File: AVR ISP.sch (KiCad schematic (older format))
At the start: 12 parts, among them CON1 AVR-ISP-6, IC1 ATMEGA328-P, IC2 ATTINY2313-P, IC3 ATTINY85-M, IC4 ATTINY2313-S

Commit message: Modified Schematic
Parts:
- removed IC3: ATTINY85-M, QFN/MLF20, symbol ATTINY85-M
- added IC3: ATTINY85-S, SO8-200, symbol ATTINY85-S
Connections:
- net +5V: now also IC3.8 (VCC)
- net GND: now also SHIELD1.GND3, IC3.4 (GND)
- net at CON1.5, IC1.1 ((PCINT14/~RESET~)PC6), IC2.1 (PA2(~RESET~/dW))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: now also IC3.1 (PB5(~RESET~/dW/ADC0/PCINT5))
- net at CON1.4, IC1.17 ((PCINT3/OC2A/MOSI)PB3), IC2.17 ((PCINT5/MOSI/DI/SDA)PB5)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: now also IC3.5 (PB0(MOSI/DI/SDA/AIN0/OC0A/OC1A/AREF/PCINT0))
- net at CON1.1, IC1.18 ((PCINT4/MISO)PB4), IC2.18 ((PCINT6/MISO/DO)PB6)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: now also IC3.6 (PB1(MISO/DO/AIN1/OC0B/OC1A/PCINT1))
- net at CON1.3, IC1.19 ((PCINT5/SCK)PB5), IC2.19 ((PCINT7/USCK/SCK/SCL)PB7)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: now also IC3.7 (PB2(SCK/USCK/SCL/T0/INT0/ADC1/PCINT2))
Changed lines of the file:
@@
-EESchema Schematic File Version 2  date 25/08/2013 21:04:07
+EESchema Schematic File Version 2  date 25/08/2013 22:06:19
 LIBS:power
 LIBS:device
@@
 Comment4 ""
 $EndDescr
+$Comp
+L GND #PWR01
+U 1 1 521A6D91
+P 6500 3800
+F 0 "#PWR01" H 6500 3800 30  0001 C CNN
+F 1 "GND" H 6500 3730 30  0001 C CNN
+	1    6500 3800
+	1    0    0    -1
+$EndComp
+$Comp
+L ATTINY85-S IC3
+U 1 1 521A67A5
+P 7800 2050
+F 0 "IC3" H 7900 2100 60  0000 C CNN
+F 1 "ATTINY85-S" H 9800 1300 60  0000 C CNN
+F 2 "SO8-200" H 8050 1300 60  0001 C CNN
+	1    7800 2050
+	1    0    0    -1
+$EndComp
 Wire Wire Line
 	4975 5950 4675 5950
@@
 	4775 5850 4975 5850
 $Comp
-L GND #PWR01
+L GND #PWR02
 U 1 1 521A5EF9
 P 5550 6100
-F 0 "#PWR01" H 5550 6100 30  0001 C CNN
+F 0 "#PWR02" H 5550 6100 30  0001 C CNN
 F 1 "GND" H 5550 6030 30  0001 C CNN
 	1    5550 6100
@@
 $EndComp
 $Comp
-L GND #PWR02
+L GND #PWR03
 U 1 1 521A5EEF
 P 4050 4500
-F 0 "#PWR02" H 4050 4500 30  0001 C CNN
+F 0 "#PWR03" H 4050 4500 30  0001 C CNN
 F 1 "GND" H 4050 4430 30  0001 C CNN
 	1    4050 4500
@@
 $EndComp
 $Comp
-L +5V #PWR03
+L +5V #PWR04
 U 1 1 521A5E82
 P 4450 3500
-F 0 "#PWR03" H 4450 3590 20  0001 C CNN
+F 0 "#PWR04" H 4450 3590 20  0001 C CNN
 F 1 "+5V" H 4450 3590 30  0000 C CNN
 	1    4450 3500
@@
 $EndComp
 $Comp
-L GND #PWR04
+L GND #PWR05
 U 1 1 521A5CF9
 P 3100 3100
-F 0 "#PWR04" H 3100 3100 30  0001 C CNN
+F 0 "#PWR05" H 3100 3100 30  0001 C CNN
 F 1 "GND" H 3100 3030 30  0001 C CNN
 	1    3100 3100
@@
 $EndComp
 $Comp
-L GND #PWR05
+L GND #PWR06
 U 1 1 521A5CF4
 P 6050 3100
-F 0 "#PWR05" H 6050 3100 30  0001 C CNN
+F 0 "#PWR06" H 6050 3100 30  0001 C CNN
 F 1 "GND" H 6050 3030 30  0001 C CNN
 	1    6050 3100
@@
 $EndComp
 $Comp
-L GND #PWR06
+L GND #PWR07
 U 1 1 521A5CED
 P 10300 2650
-F 0 "#PWR06" H 10300 2650 30  0001 C CNN
+F 0 "#PWR07" H 10300 2650 30  0001 C CNN
 F 1 "GND" H 10300 2580 30  0001 C CNN
 	1    10300 2650
@@
 $EndComp
 $Comp
-L GND #PWR07
+L GND #PWR08
 U 1 1 521A5B0E
 P 8550 5800
-F 0 "#PWR07" H 8550 5800 30  0001 C CNN
+F 0 "#PWR08" H 8550 5800 30  0001 C CNN
 F 1 "GND" H 8550 5730 30  0001 C CNN
 	1    8550 5800
@@
 $EndComp
 $Comp
-L GND #PWR08
+L GND #PWR09
 U 1 1 521A5B08
 P 8550 5700
-F 0 "#PWR08" H 8550 5700 30  0001 C CNN
+F 0 "#PWR09" H 8550 5700 30  0001 C CNN
 F 1 "GND" H 8550 5630 30  0001 C CNN
 	1    8550 5700
@@
 $EndComp
 $Comp
-L GND #PWR09
+L GND #PWR010
 U 1 1 521A5B03
 P 8000 5000
-F 0 "#PWR09" H 8000 5000 30  0001 C CNN
+F 0 "#PWR010" H 8000 5000 30  0001 C CNN
 F 1 "GND" H 8000 4930 30  0001 C CNN
 	1    8000 5000
@@
 $EndComp
 $Comp
-L GND #PWR010
+L GND #PWR011
 U 1 1 521A5AFA
 P 8000 4700
-F 0 "#PWR010" H 8000 4700 30  0001 C CNN
+F 0 "#PWR011" H 8000 4700 30  0001 C CNN
 F 1 "GND" H 8000 4630 30  0001 C CNN
 	1    8000 4700
@@
 $EndComp
 $Comp
-L GND #PWR011
+L GND #PWR012
 U 1 1 521A5AF3
 P 8000 4400
-F 0 "#PWR011" H 8000 4400 30  0001 C CNN
+F 0 "#PWR012" H 8000 4400 30  0001 C CNN
 F 1 "GND" H 8000 4330 30  0001 C CNN
 	1    8000 4400
@@
 	1    0    0    -1
 $EndComp
-$Comp
-L ATTINY85-M IC3
-U 1 1 520B9E29
-P 7800 2050
-F 0 "IC3" H 7900 2100 60  0000 C CNN
-F 1 "ATTINY85-M" H 9800 1300 60  0000 C CNN
-F 2 "QFN/MLF20" H 8100 1300 60  0001 C CNN
-	1    7800 2050
-	1    0    0    -1
-$EndComp

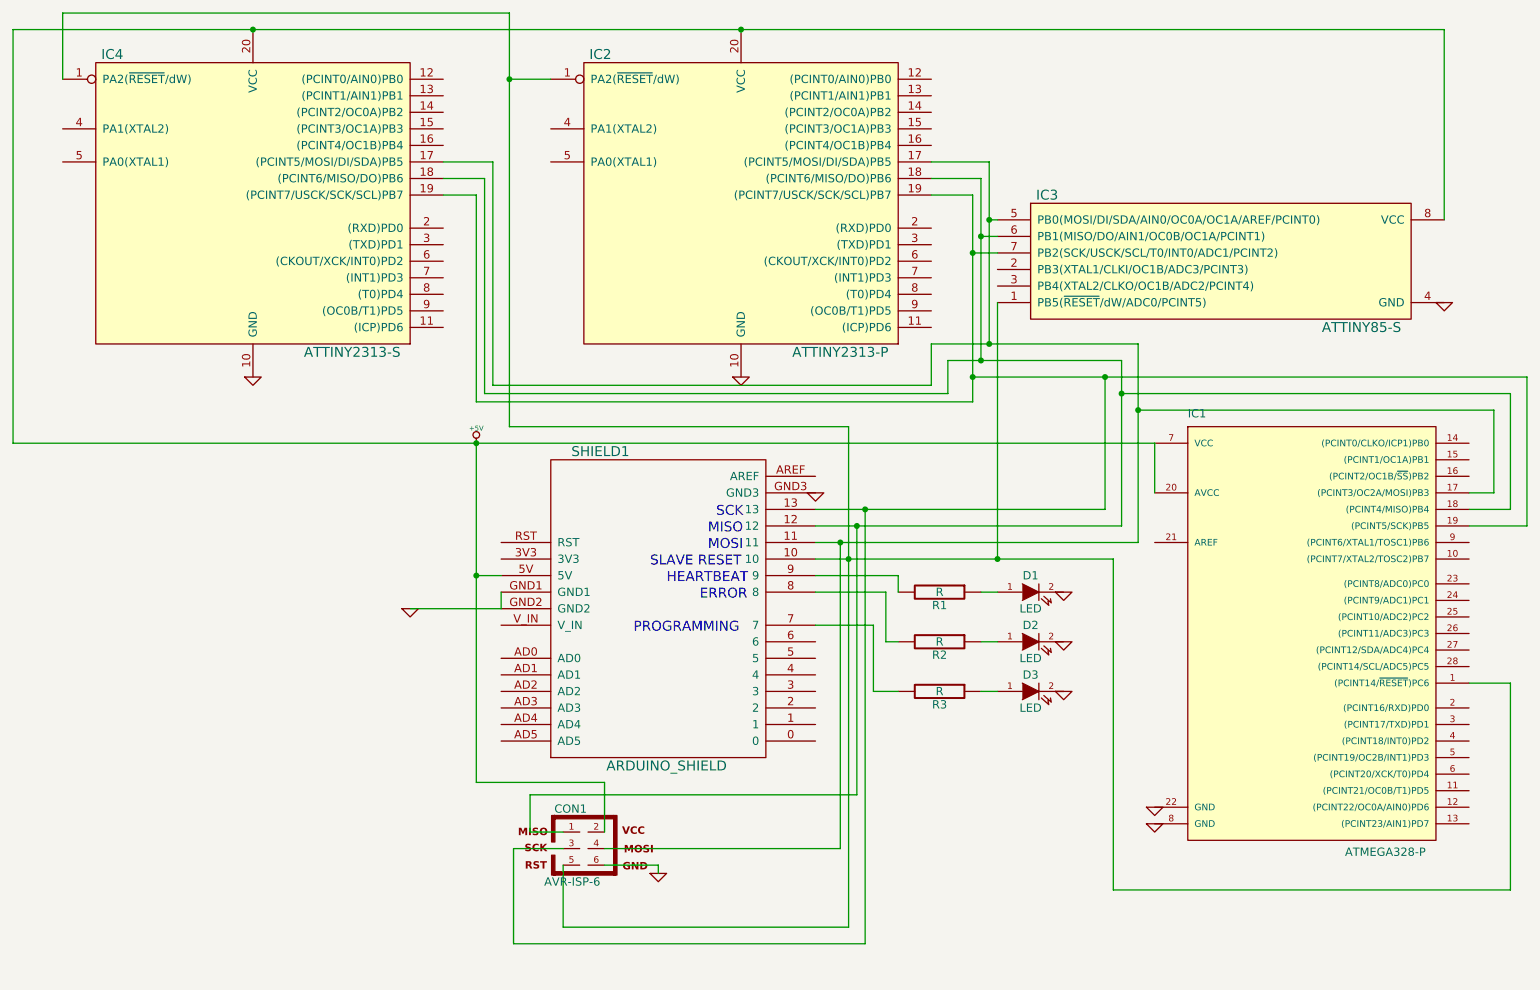
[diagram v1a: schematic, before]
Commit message: Logos added and ATTiny85 Moved.
Also added ground to the soic at pin 4 for ATTiny85 programming and
moved the ISP Headers to allow me to put a massive logo on the back.
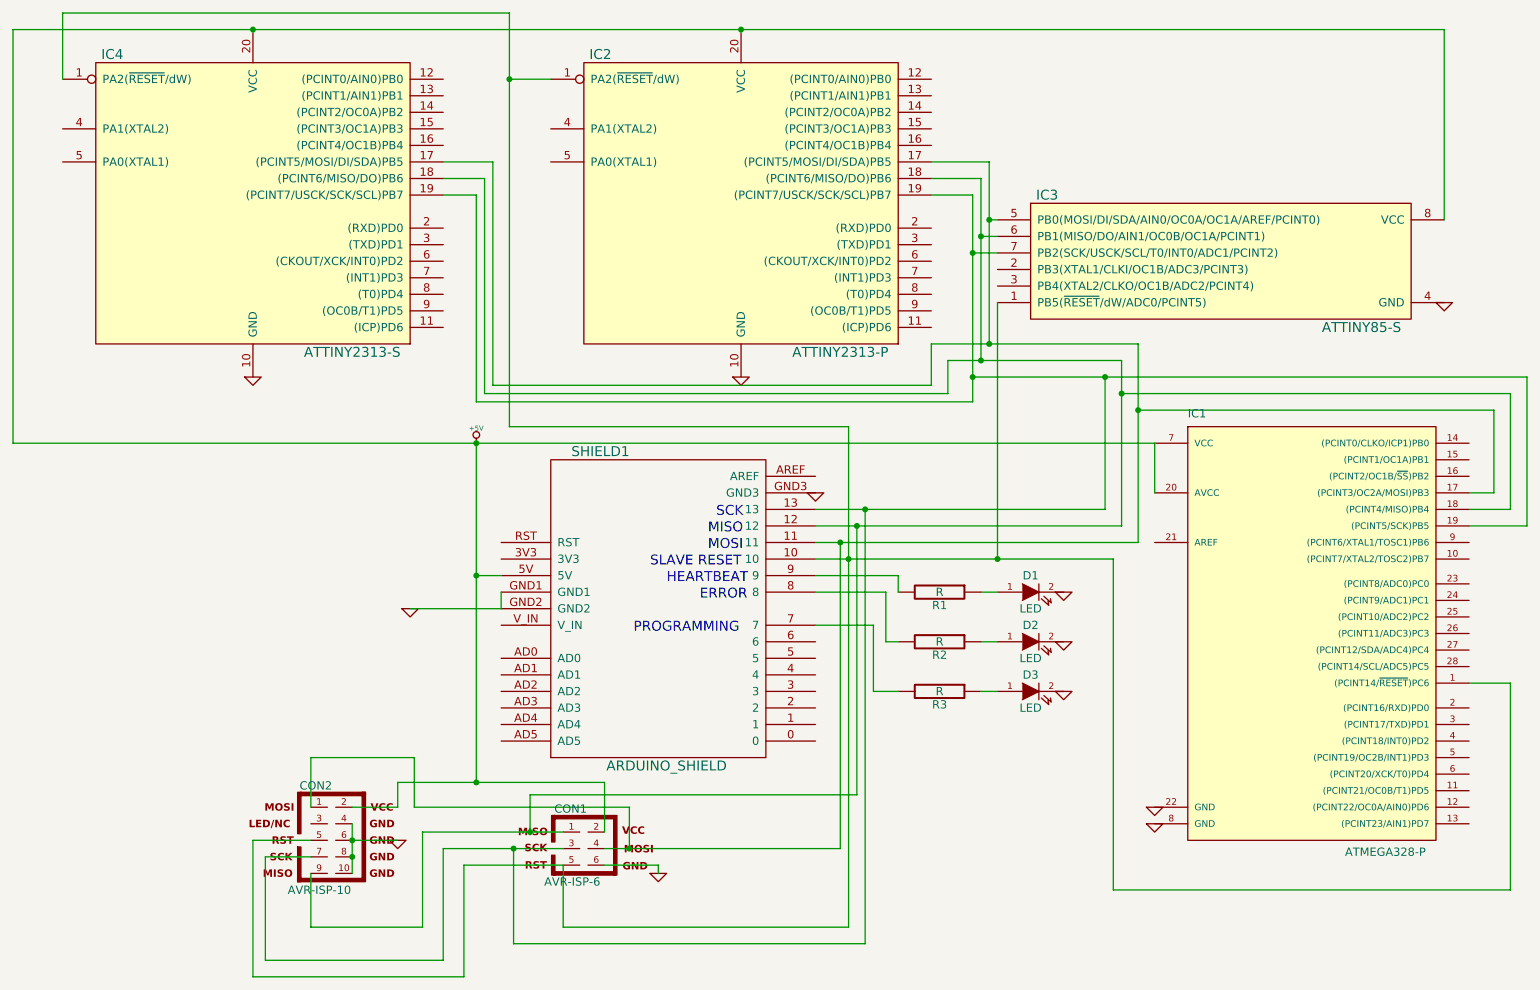
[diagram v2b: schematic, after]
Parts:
- added CON2: AVR-ISP-10, AVR-ISP-10, symbol AVR-ISP-10
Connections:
- net +5V: now also CON2.2
- net GND: now also CON2.10, CON2.4, CON2.6, CON2.8
- net at CON1.5, IC1.1 ((PCINT14/~RESET~)PC6), IC2.1 (PA2(~RESET~/dW))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: now also CON2.5
- net at CON1.4, IC1.17 ((PCINT3/OC2A/MOSI)PB3), IC2.17 ((PCINT5/MOSI/DI/SDA)PB5)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: now also CON2.1
- net at CON1.1, IC1.18 ((PCINT4/MISO)PB4), IC2.18 ((PCINT6/MISO/DO)PB6)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: now also CON2.9
- net at CON1.3, IC1.19 ((PCINT5/SCK)PB5), IC2.19 ((PCINT7/USCK/SCK/SCL)PB7)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: now also CON2.7
